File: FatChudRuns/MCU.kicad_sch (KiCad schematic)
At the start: 18 parts, among them J2 Conn_02x20_Odd_Even, J3 FTSH-107-01-L-DV-K-P, SW1 SW_Push, SW2 SW_DIP_x01, U1 STM32F107RBTx

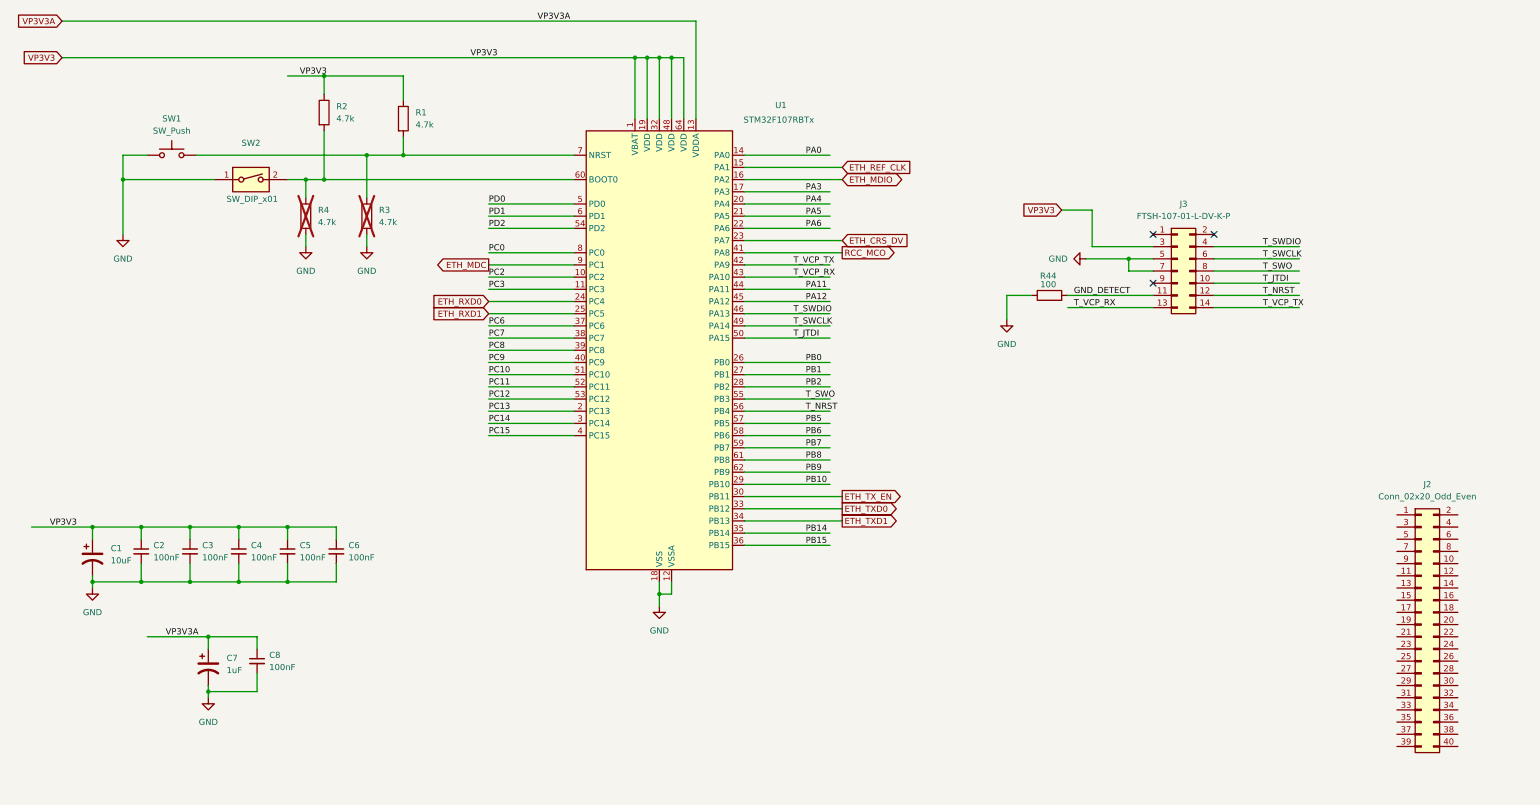
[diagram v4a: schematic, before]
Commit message: connected remaining gpio pins to connector, added kicad power pins instead of net names
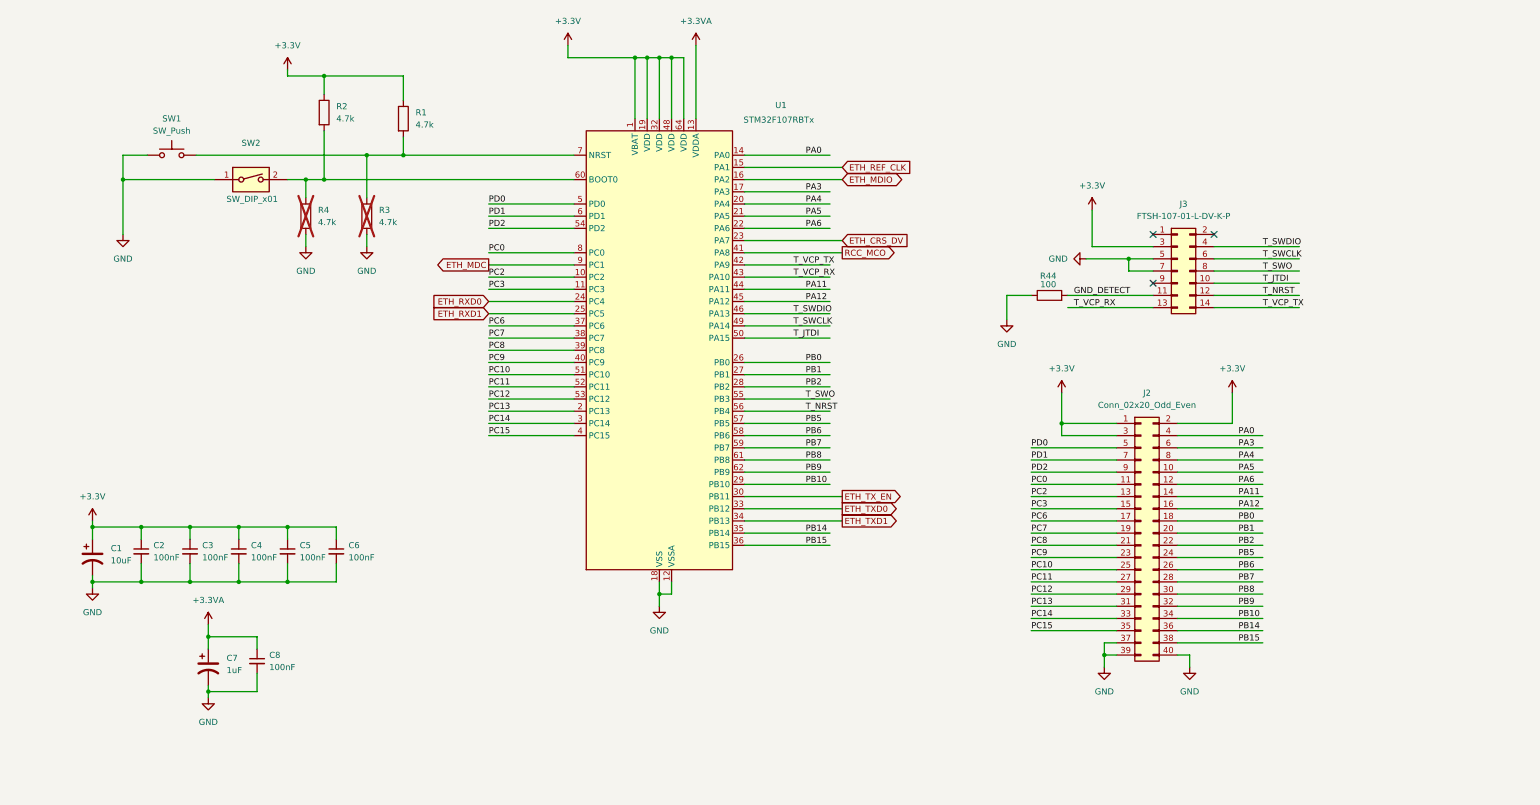
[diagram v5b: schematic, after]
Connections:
- net VP3V3 is gone; now on net +3.3V: C1.1, C2.1, C3.1, C4.1, C5.1, C6.1, J3.3 (Pin_3), R1.1, R2.1, U1.1 (VBAT), U1.19 (VDD), U1.32 (VDD), U1.48 (VDD), U1.64 (VDD)
- net GND: now also J2.37 (Pin_37), J2.39 (Pin_39), J2.40 (Pin_40)
- net PA0: now also J2.4 (Pin_4)
- net PA11: now also J2.14 (Pin_14)
- net PA12: now also J2.16 (Pin_16)
- net PA3: now also J2.6 (Pin_6)
- net PA4: now also J2.8 (Pin_8)
- net PA5: now also J2.10 (Pin_10)
- net PA6: now also J2.12 (Pin_12)
- net PB0: now also J2.18 (Pin_18)
- net PB1: now also J2.20 (Pin_20)
- net PB10: now also J2.34 (Pin_34)
- net PB14: now also J2.36 (Pin_36)
- net PB15: now also J2.38 (Pin_38)
- net PB2: now also J2.22 (Pin_22)
- net PB5: now also J2.24 (Pin_24)
- net PB6: now also J2.26 (Pin_26)
- net PB7: now also J2.28 (Pin_28)
- net PB8: now also J2.30 (Pin_30)
- net PB9: now also J2.32 (Pin_32)
- net PC0: now also J2.11 (Pin_11)
- net PC10: now also J2.25 (Pin_25)
- net PC11: now also J2.27 (Pin_27)
- net PC12: now also J2.29 (Pin_29)
- net PC13: now also J2.31 (Pin_31)
- net PC14: now also J2.33 (Pin_33)
- net PC15: now also J2.35 (Pin_35)
- net PC2: now also J2.13 (Pin_13)
- net PC3: now also J2.15 (Pin_15)
- net PC6: now also J2.17 (Pin_17)
- net PC7: now also J2.19 (Pin_19)
- net PC8: now also J2.21 (Pin_21)
- net PC9: now also J2.23 (Pin_23)
- net PD0: now also J2.5 (Pin_5)
- net PD1: now also J2.7 (Pin_7)
- net PD2: now also J2.9 (Pin_9)
- net +3.3V: now reaches J2.1 (Pin_1)
- net +3.3V: now also J2.2 (Pin_2), J2.3 (Pin_3)
- net VP3V3A renamed +3.3VA
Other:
- moved on the sheet: J2

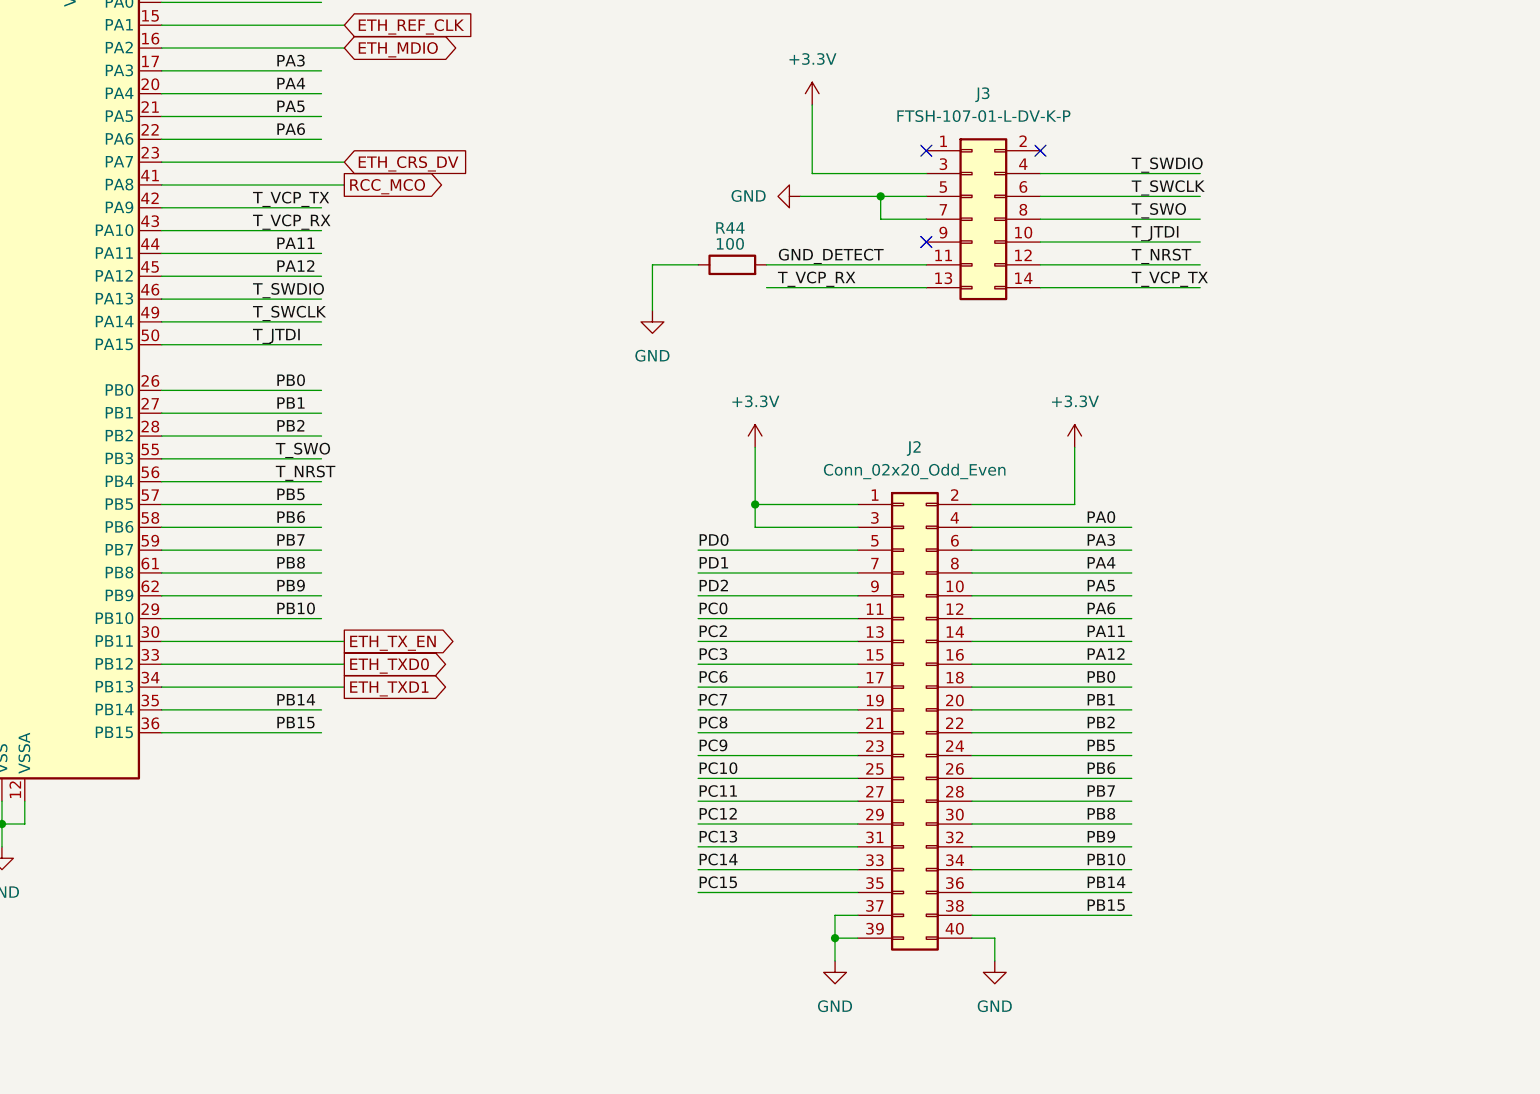
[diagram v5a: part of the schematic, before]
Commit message: add usb c power circuitry, added led for power indication, increased resistance of ethernet leds light to 220ohms
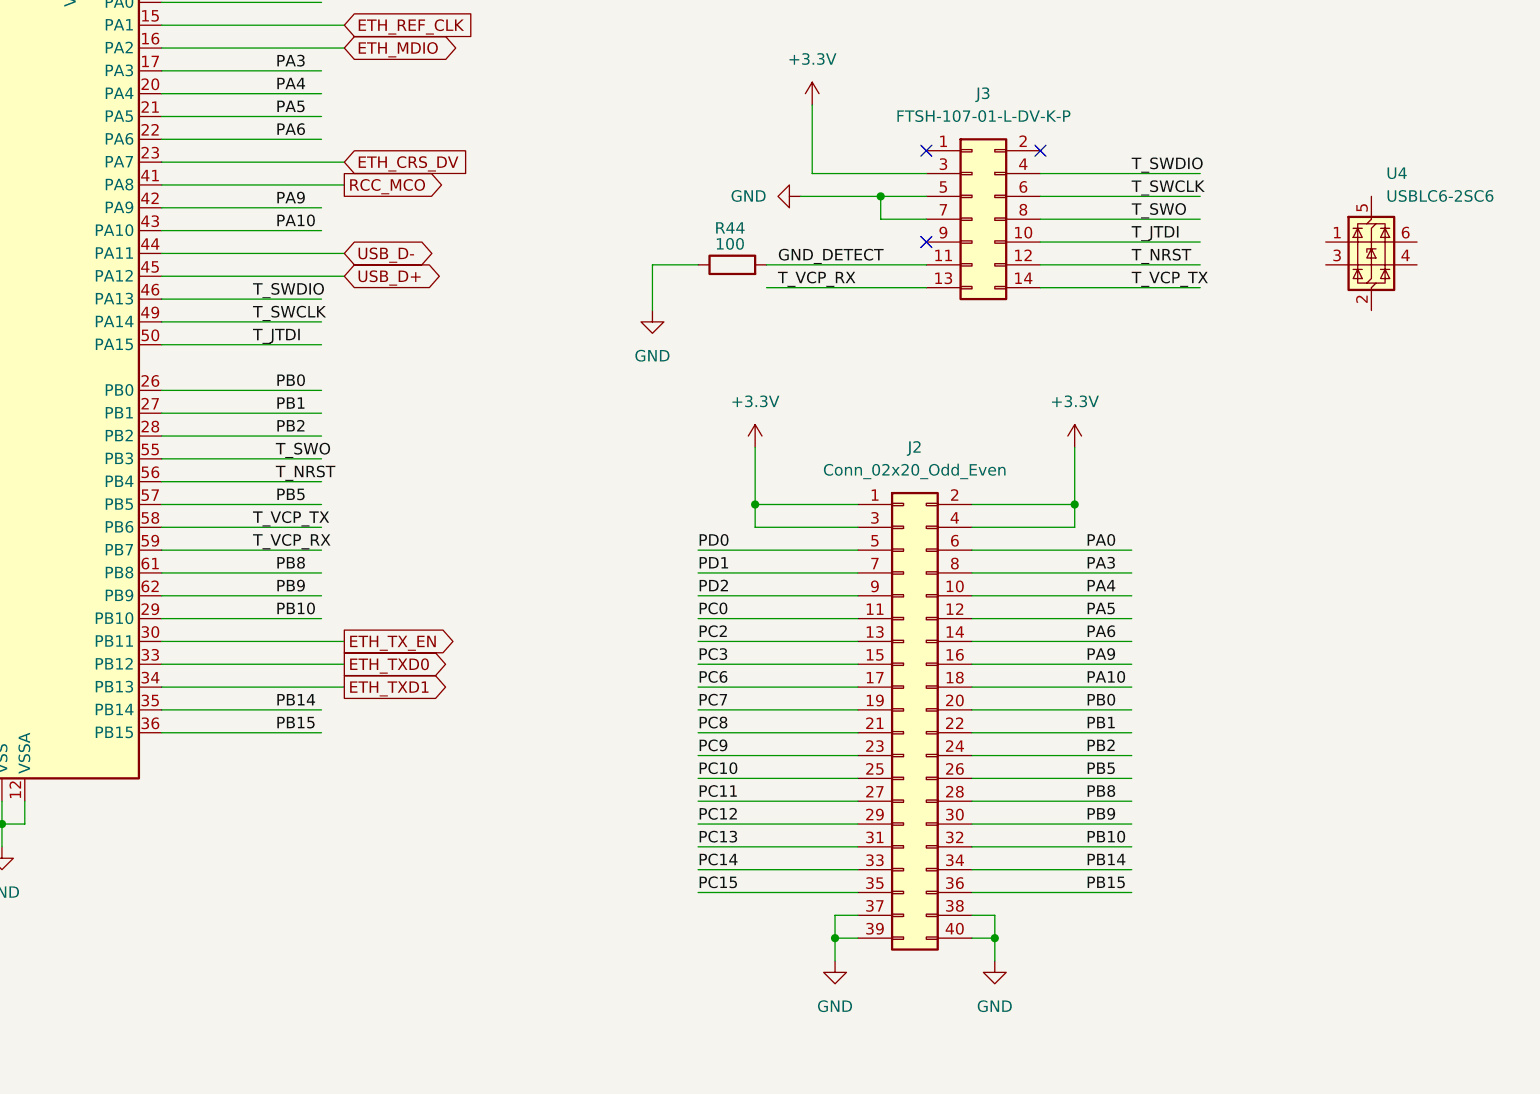
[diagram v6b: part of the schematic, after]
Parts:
- added U4: USBLC6-2SC6, Package_TO_SOT_SMD:SOT-23-6, symbol Power_Protection:USBLC6-2SC6
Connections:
- net +3.3V: now also J2.4 (Pin_4)
- net GND: now also J2.38 (Pin_38)
- net PA0: now also J2.6 (Pin_6); no longer J2.4 (Pin_4)
- net PA3: now also J2.8 (Pin_8); no longer J2.6 (Pin_6)
- net PA4: now also J2.10 (Pin_10); no longer J2.8 (Pin_8)
- net PA5: now also J2.12 (Pin_12); no longer J2.10 (Pin_10)
- net PA6: now also J2.14 (Pin_14); no longer J2.12 (Pin_12)
- net PB0: now also J2.20 (Pin_20); no longer J2.18 (Pin_18)
- net PB1: now also J2.22 (Pin_22); no longer J2.20 (Pin_20)
- net PB10: now also J2.32 (Pin_32); no longer J2.34 (Pin_34)
- net PB14: now also J2.34 (Pin_34); no longer J2.36 (Pin_36)
- net PB15: now also J2.36 (Pin_36); no longer J2.38 (Pin_38)
- net PB2: now also J2.24 (Pin_24); no longer J2.22 (Pin_22)
- net PB5: now also J2.26 (Pin_26); no longer J2.24 (Pin_24)
- net PB8: now also J2.28 (Pin_28); no longer J2.30 (Pin_30)
- net PB9: now also J2.30 (Pin_30); no longer J2.32 (Pin_32)
- net T_VCP_RX: now also U1.59 (PB7); no longer U1.43 (PA10)
- net T_VCP_TX: now also U1.58 (PB6); no longer U1.42 (PA9)
- net PA11 renamed USB_D-
- net USB_D-: no longer J2.14 (Pin_14)
- net PA12 renamed PA9
- net PA9: now also U1.42 (PA9); no longer U1.45 (PA12)
- removed net PB6: J2.26 (Pin_26), U1.58 (PB6)
- removed net PB7: J2.28 (Pin_28), U1.59 (PB7)
- new net PA10: J2.18 (Pin_18), U1.43 (PA10)
- new net USB_D+: U1.45 (PA12)

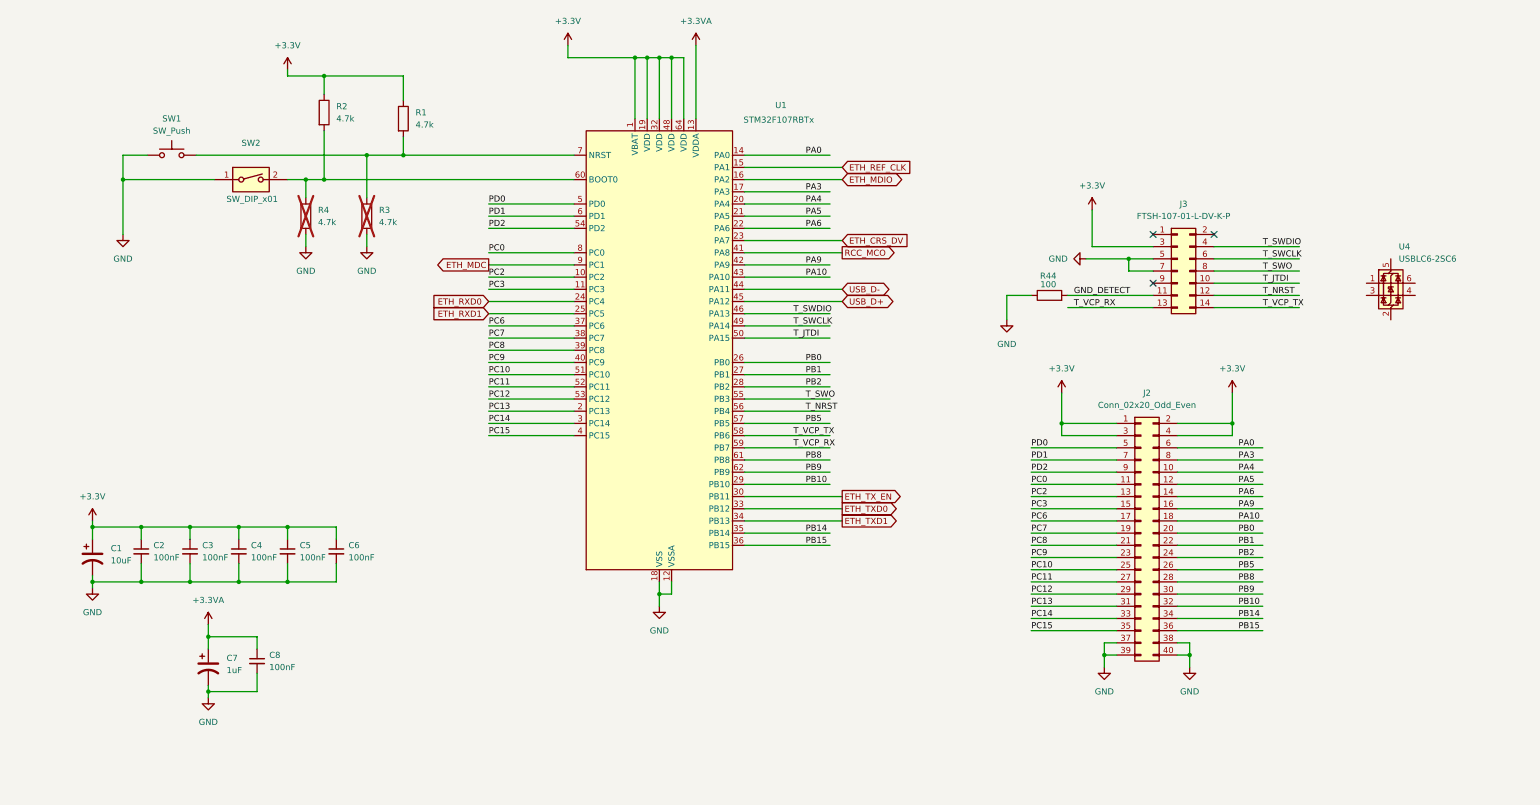
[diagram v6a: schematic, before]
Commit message: sorted out erc errors and warning, connected tvs diodes to jtag
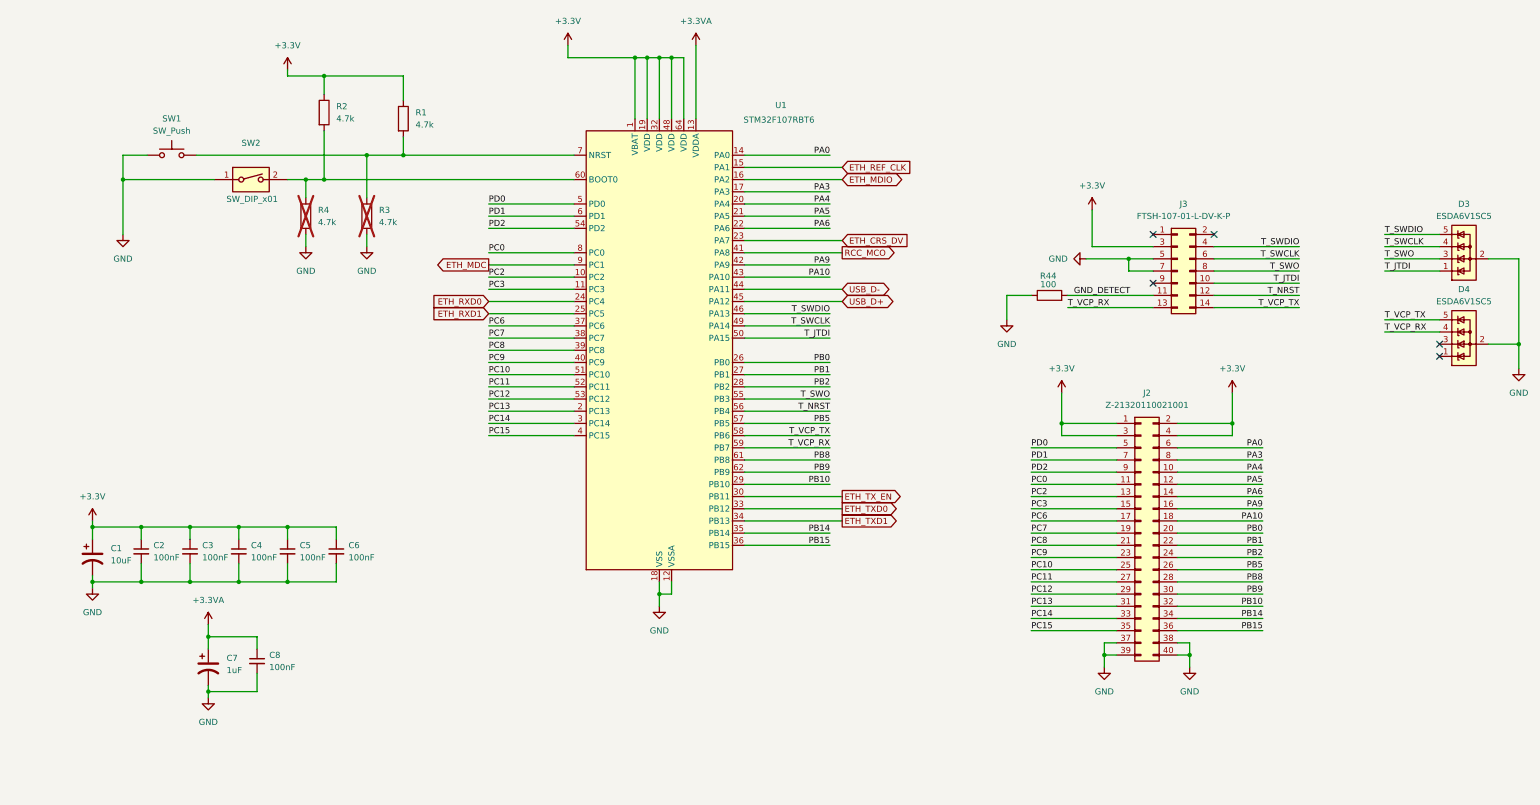
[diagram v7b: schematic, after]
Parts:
- removed U4: USBLC6-2SC6, Package_TO_SOT_SMD:SOT-23-6, symbol Power_Protection:USBLC6-2SC6
- added D3, D4: ESDA6V1SC5, Package_TO_SOT_SMD:SOT-23-5, symbol Power_Protection:ESDA6V1SC5
- J2: value Conn_02x20_Odd_Even -> Z-21320110021001
- U1: value STM32F107RBTx -> STM32F107RBT6
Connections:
- net GND: now also D3.2 (A), D4.2 (A)
- net T_JTDI: now also D3.1 (K)
- net T_SWCLK: now also D3.4 (K)
- net T_SWDIO: now also D3.5 (K)
- net T_SWO: now also D3.3 (K)
- net T_VCP_RX: now also D4.4 (K)
- net T_VCP_TX: now also D4.5 (K)
- no-connect marks 3 -> 5
